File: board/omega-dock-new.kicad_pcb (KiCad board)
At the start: 2 copper layers, 42.9 x 26.4 mm, 18 parts, among them J1 USB_A, J2 USB_PWR, J3 RJ45-TRANSFO, U1 USBLC6-2, U2 AP111733, U3 OMEGA_2

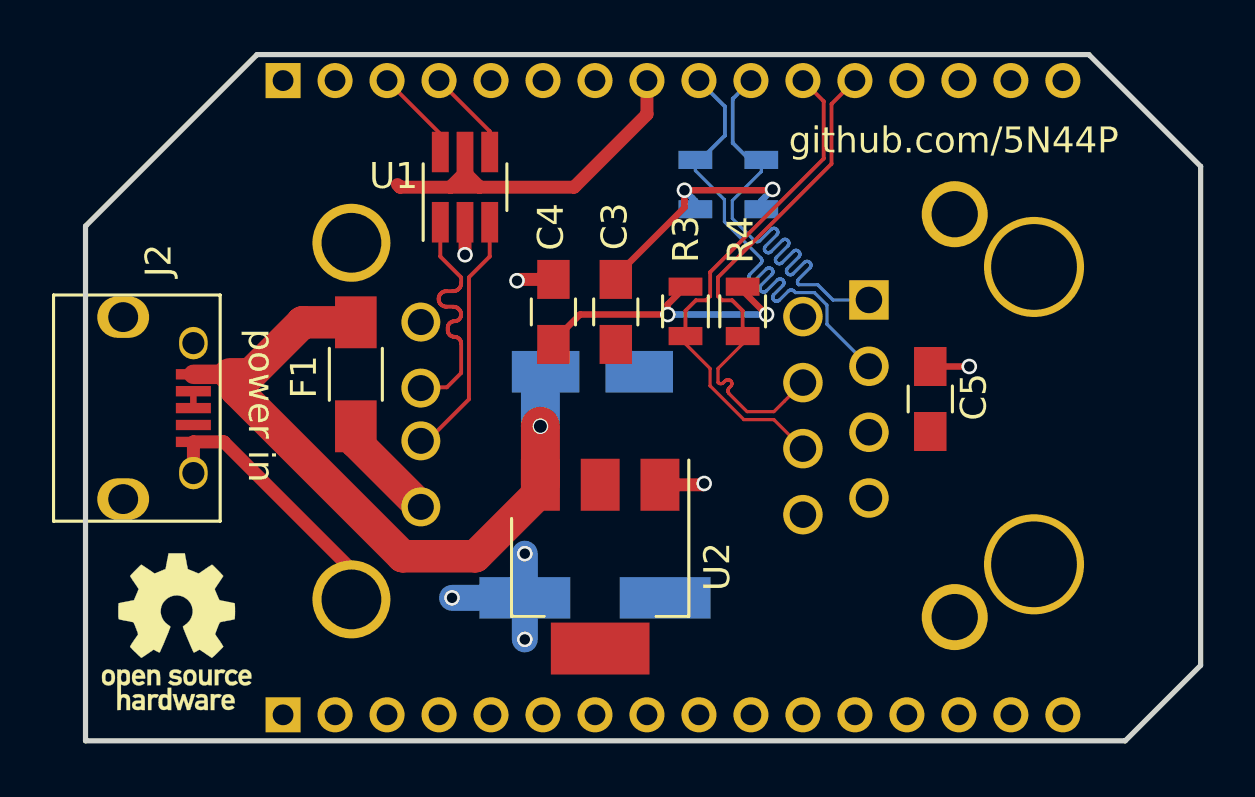
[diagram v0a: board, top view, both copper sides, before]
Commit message: v1.0 fixes #1, fixes #2, fixes #3, fixes #4, fixes #5, fixes #7, fixes #8
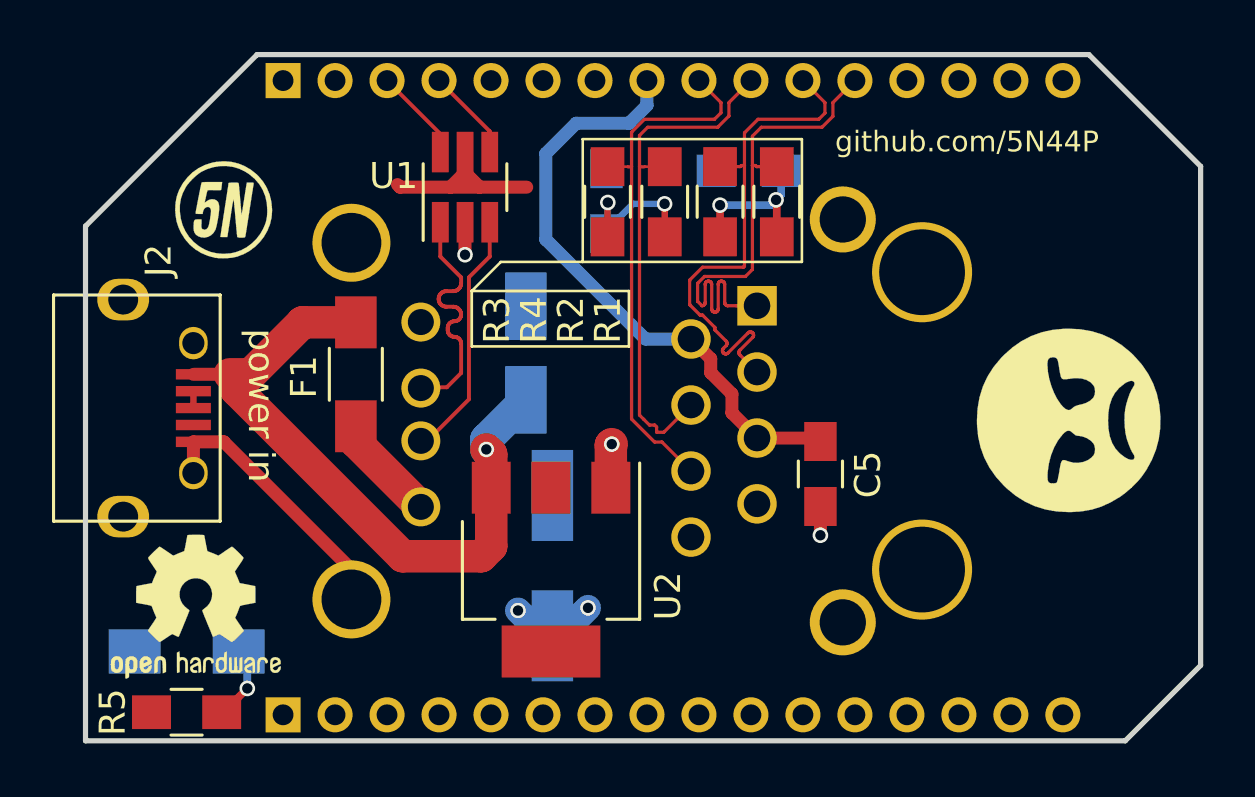
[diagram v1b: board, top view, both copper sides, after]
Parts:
- removed the REF*** at (157.6, 66.7)
- added D1: PWR, LEDs:LED_1206_HandSoldering, B.Cu at (158.0, 67.5)
- added G***: LOGO, logo:LOGO_5N, F.Cu at (159.6, 50.5)
- added R5: 150R, Resistors_SMD:R_0805_HandSoldering, F.Cu at (158.0, 69.8)
- added REF***: OSHW-Logo2_7.3x6mm_SilkScreen, Symbols:OSHW-Logo2_7.3x6mm_SilkScreen, F.Cu at (158.3, 65.7)
- C3, C4: moved to B.Cu
- G***: moved to F.Cu
- J3: value RJ45-TRANSFO -> RJ45-TRAFO; footprint omega:RJ45_TRAfo -> RJ45-TRAFO-AMPHENOL:RJ45_TRAFO_AMPHENOL
- R1, R2: footprint Resistors_SMD:R_0805 -> Resistors_SMD:R_0805_HandSoldering; moved to F.Cu
- R3, R4: footprint Resistors_SMD:R_0805 -> Resistors_SMD:R_0805_HandSoldering
- moved G*** 36.1 mm to (191.9, 58.6), turned to 90 degrees
- moved C3 7.45 mm to (179.6, 49.0), turned to 0 degrees
- moved R3 5.17 mm to (174.2, 50.2), turned to 270 degrees
- moved R4 5.17 mm to (176.4, 50.2), turned to 270 degrees
- moved C5 5.12 mm to (182.4, 60.6), turned to 270 degrees
- moved C4 4.72 mm to (174.1, 50.1)
- moved J3 4.31 mm to (177.4, 62.4)
- moved C1 2.66 mm to (171.0, 56.0), turned to 90 degrees
- moved C2 2.06 mm to (172.1, 64.2), turned to 90 degrees
- moved U2 1.89 mm to (172.0, 64.3)
- moved R2 1.16 mm to (178.5, 50.2)
- moved R1 0.89 mm to (180.7, 50.2)
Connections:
- net GNDPWR renamed Net-(J3-Pad13)
- C5 pad 1: +3V3 -> ETH_PWR
- J2 pad 4: (no net) -> Net-(J2-Pad4)
- J3 pad 1: /TX+ -> /RX+
- J3 pad 2: +3V3 -> ETH_PWR
- J3 pad 3: /TX- -> /RX-
- J3 pad 4: /RX+ -> /TX+
- J3 pad 5: +3V3 -> ETH_PWR
- J3 pad 6: /RX- -> /TX-
- R1 pad 2: /TX+ -> /RX+
- R2 pad 2: /TX- -> /RX-
- R3 pad 1: /RX- -> /TX-
- R4 pad 1: /RX+ -> /TX+
- U3 pad 10: (no net) -> Net-(U3-Pad10)
- U3 pad 11: (no net) -> Net-(U3-Pad11)
- U3 pad 12: (no net) -> Net-(U3-Pad12)
- U3 pad 13: (no net) -> Net-(U3-Pad13)
- U3 pad 14: (no net) -> Net-(U3-Pad14)
- U3 pad 15: (no net) -> Net-(U3-Pad15)
- U3 pad 16: (no net) -> Net-(U3-Pad16)
- U3 pad 17: (no net) -> Net-(U3-Pad17)
- U3 pad 18: (no net) -> Net-(U3-Pad18)
- U3 pad 19: (no net) -> Net-(U3-Pad19)
- U3 pad 2: (no net) -> Net-(U3-Pad2)
- U3 pad 20: (no net) -> Net-(U3-Pad20)
- U3 pad 25: +3V3 -> ETH_PWR
- U3 pad 26: (no net) -> Net-(U3-Pad26)
- U3 pad 27: (no net) -> Net-(U3-Pad27)
- U3 pad 28: (no net) -> Net-(U3-Pad28)
- U3 pad 3: (no net) -> Net-(U3-Pad3)
- U3 pad 4: (no net) -> Net-(U3-Pad4)
- U3 pad 5: (no net) -> Net-(U3-Pad5)
- U3 pad 6: (no net) -> Net-(U3-Pad6)
- U3 pad 7: (no net) -> Net-(U3-Pad7)
- U3 pad 8: (no net) -> Net-(U3-Pad8)
- U3 pad 9: (no net) -> Net-(U3-Pad9)
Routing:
- net ETH_PWR: track 0.00 -> 23.4 mm
- net +3V3: track 21.4 -> 10.9 mm, vias 3 -> 2
- net Net-(C4-Pad1): track 11.6 -> 6.60 mm
- net Net-(C3-Pad2): track 9.78 -> 6.09 mm
- net Net-(D1-Pad2): track 0.00 -> 3.29 mm, vias 0 -> 1
- net GND: track 16.4 -> 14.5 mm, vias 4 -> 3
- net /RX-: track 20.0 -> 21.5 mm
- net /RX+: track 19.5 -> 20.7 mm
- net +5V: track 27.9 -> 26.8 mm
- net /TX-: track 19.9 -> 20.4 mm
